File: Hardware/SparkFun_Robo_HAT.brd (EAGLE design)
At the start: 65 x 56.5 mm, 236 parts, among them J11 EXT MTR PWR, J18 ISP, J2 RASPBERRYPI-40-PIN-GPIO_PTH_N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, J20 USB C, J23 CORTEX_JTAG_DEBUG_PTH, J7 EXT SERVO PWR, J8 EXT 5V PWR, Q1 310mA/60V/1.6Ω, Q23 20V/0.2A/8MHz/1.2Ω/1Vth, Q24 20V/0.2A/8MHz/1.2Ω/1Vth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

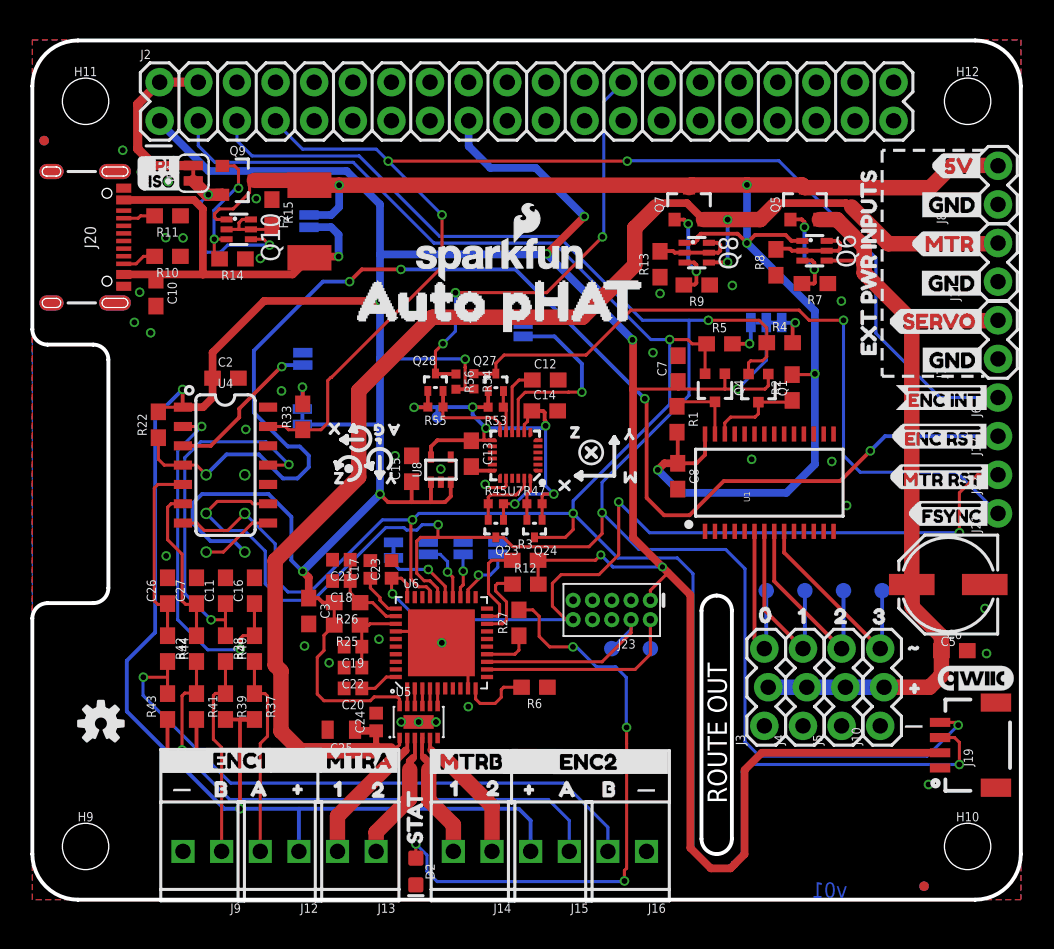
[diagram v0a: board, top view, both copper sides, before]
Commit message: post double-check changes - ready for proto v01
-moved TP6 to SMT pad style and on grid
-updated tran-14386 (ideal diode) to have polarity mark outside package
-nudged vias to avoid silk labels
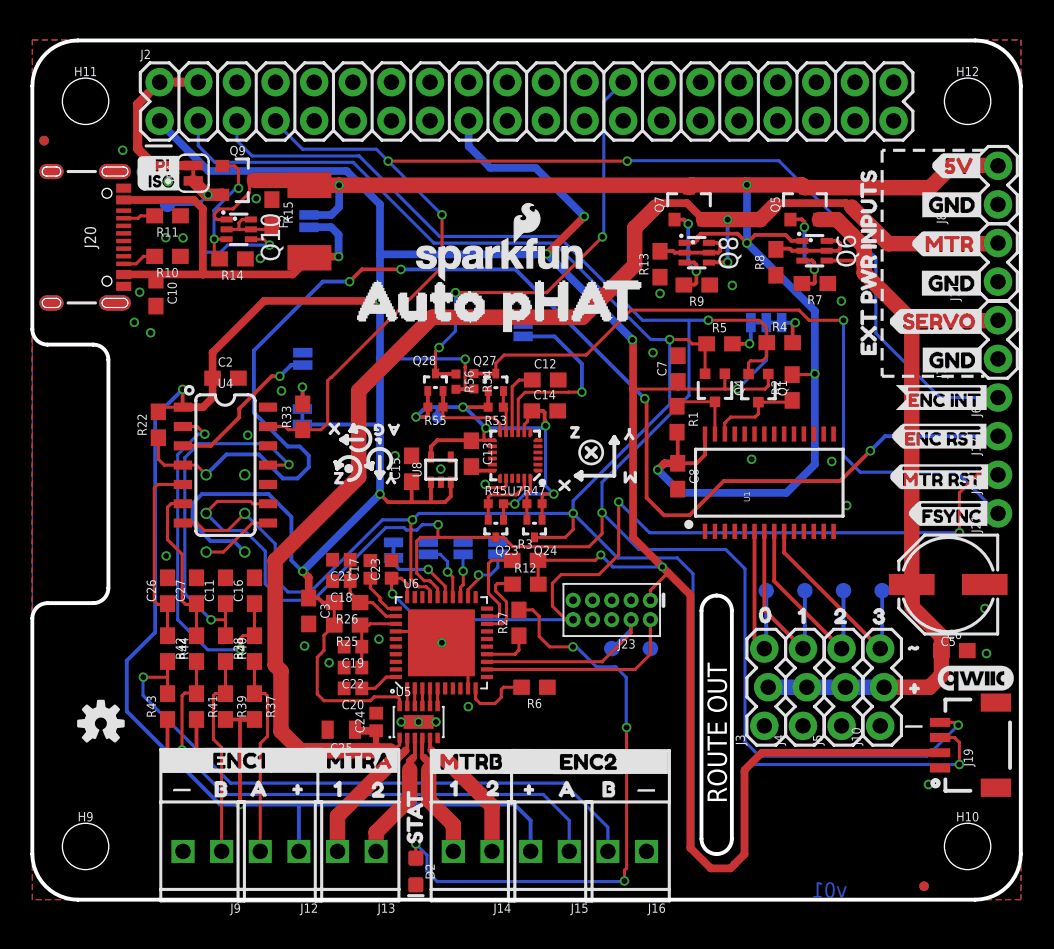
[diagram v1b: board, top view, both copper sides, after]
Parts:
- TP6: value (none) -> TEST-POINT3X4; device SparkFun-Connectors:TP_15TH -> SparkFun-Connectors:PAD.03X.04
- moved TP6 2.76 mm to (8.89, 45.7)
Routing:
- net PI-5V: track 13.1 -> 14.4 mm, vias 1 -> 2
- net 1.8V: track 35.7 -> 36.6 mm

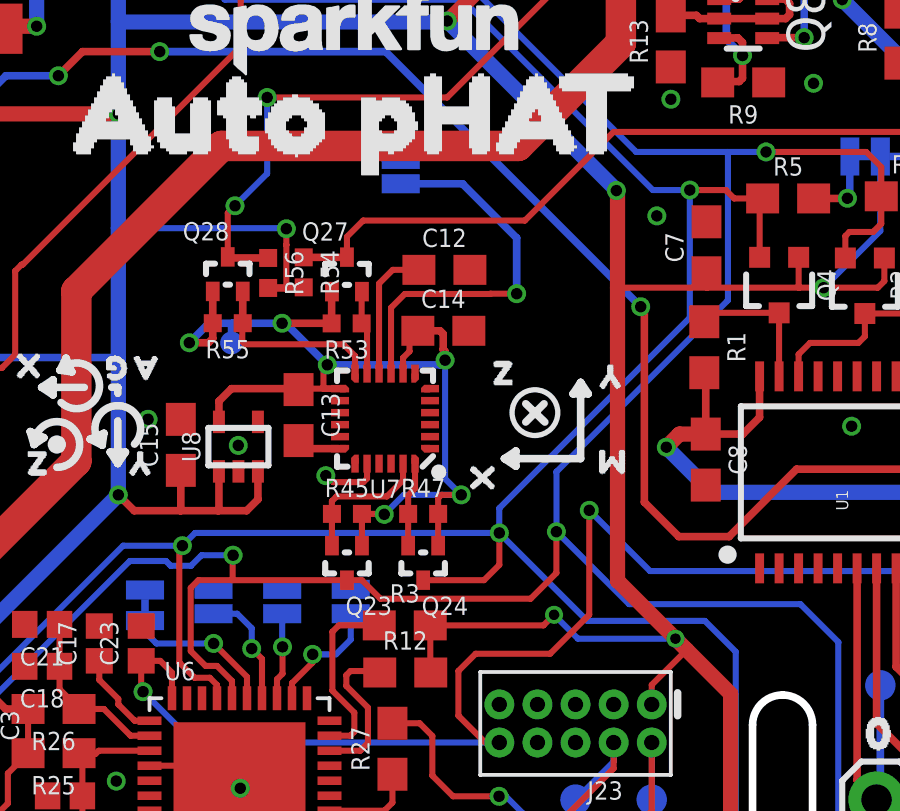
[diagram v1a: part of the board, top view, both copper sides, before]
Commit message: Connected IMU CS pin to 1.8V, Added IMU ADR PU 2.2K resistor
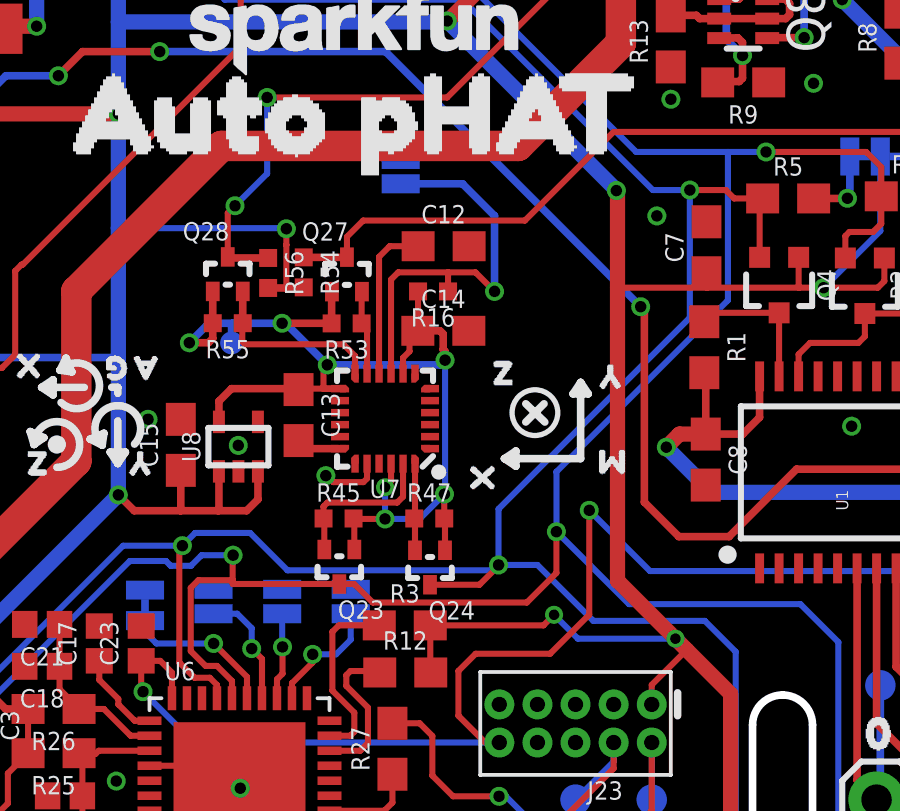
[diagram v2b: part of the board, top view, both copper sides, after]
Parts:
- added R16: 2.2k, SparkFun-Resistors:0402-TIGHT
- moved C12 0.79 mm to (33.7, 35.0)
- moved R45 0.32 mm to (30.2, 25.9)
- moved Q23 0.28 mm to (30.2, 23.7)
- moved Q24 0.27 mm to (33.2, 23.7)
- moved R47 0.25 mm to (33.2, 25.9)
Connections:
- net 1.8V: now also R16.2, U7.22
- net AD0/SDO: now also R16.1
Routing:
- net 1.8V: track 36.6 -> 38.9 mm, vias 6 -> 7
- net N$29: track 4.52 -> 5.34 mm
- net SCL_1.8V: track 4.70 -> 5.33 mm
- net AD0/SDO: track 13.1 -> 13.7 mm

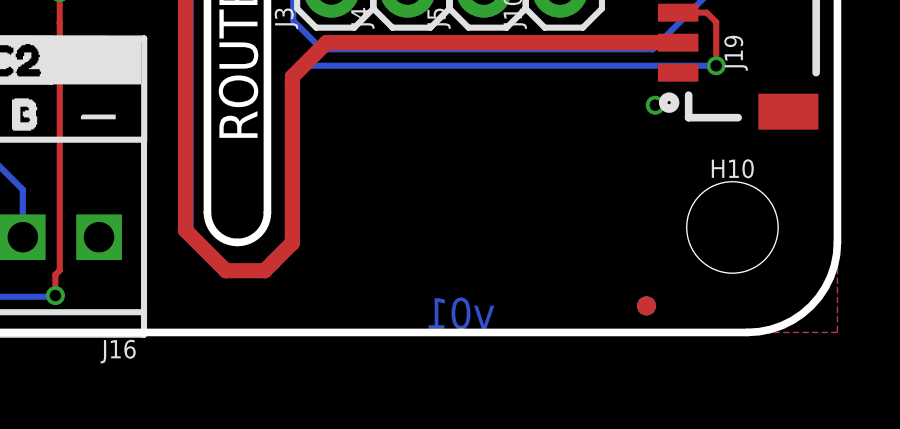
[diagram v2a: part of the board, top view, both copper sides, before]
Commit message: bumped version to v10 in sch and brd
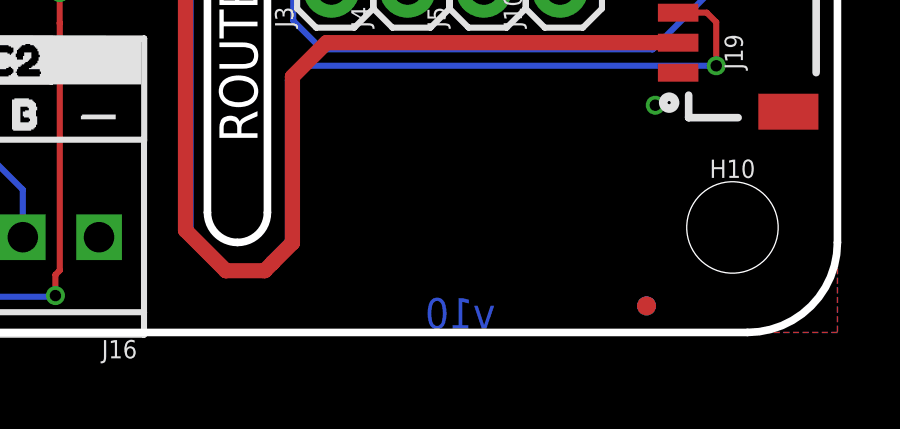
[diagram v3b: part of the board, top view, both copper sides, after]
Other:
- board text added: "v10"
- board text removed: "v01"
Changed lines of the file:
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@@
 <rectangle x1="7.40918125" y1="47.767240625" x2="7.79525625" y2="48.894996875" layer="21"/>
 <rectangle x1="9.21511875" y1="47.75708125" x2="9.65961875" y2="48.91024375" layer="21"/>
-<text x="53.594" y="0.127" size="1.016" layer="16" font="vector" ratio="20" rot="SMR0">v01</text>
+<text x="53.594" y="0.127" size="1.016" layer="16" font="vector" ratio="20" rot="SMR0">v10</text>
 <text x="45.669196875" y="6.33221875" size="1.27" layer="20" font="vector" ratio="12" rot="R90">ROUTE OUT</text>
 <circle x="20.810221875" y="28.348940625" radius="0.3048" width="0" layer="21"/>

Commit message: moving to SMD stackable solution... 99 done
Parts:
- J19: value (none) -> QWIIC_RIGHT_ANGLE; device SparkFun-Connectors:1X04_1MM_RA -> SparkFun-Connectors:JST04_1MM_RA
- J2: value RASPBERRYPI-40-PIN-GPIO_PTH_NO_SHROUD -> RASPBERRYPI-40-PIN-GPIO_SMD_STACKABLE; device SparkFun-Connectors:2X20 -> SparkFun-Connectors:RASPBERRY_PI_HAT_40_PIN_SMD_STACKABLE
- TP0, TP1, TP2, TP3, TP7, TP8: value (none) -> TEST-POINT3X4
- TP4, TP5: value (none) -> TEST-POINTTP_15TH_THRU
- TP9: value (none) -> TEST-POINT3
- moved TP6 1.27 mm to (8.89, 44.5)
- moved U$32 1.20 mm to (6.86, 46.1)
- moved U$35 1.20 mm to (7.32, 47.1)
- moved JP4 1.15 mm to (10.5, 46.6)
- moved R11 0.79 mm to (8.86, 44.2)
- moved Q9 0.69 mm to (13.5, 46.6)
- moved R15 0.27 mm to (15.9, 45.0)
- moved F2 0.23 mm to (18.2, 44.4)
- moved Q10 0.16 mm to (13.6, 43.9)
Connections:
- new net CE0: J2.24, J2.24B
- new net GP12: J2.32, J2.32B
- new net GP13: J2.33, J2.33B
- new net GP16: J2.36, J2.36B
- new net GP17: J2.11, J2.11B
- new net GP18: J2.12, J2.12B
- new net GP19: J2.35, J2.35B
- new net GP20: J2.38, J2.38B
- new net GP21: J2.40, J2.40B
- new net GP22: J2.15, J2.15B
- new net GP23: J2.16, J2.16B
- new net GP24: J2.18, J2.18B
- new net GP25: J2.22, J2.22B
- new net GP26: J2.37, J2.37B
- new net GP27: J2.13, J2.13B
- new net GP5: J2.29, J2.29B
- new net GP6: J2.31, J2.31B
- new net ID_SC: J2.28, J2.28B
- new net ID_SD: J2.27, J2.27B
- new net PI_MISO: J2.21, J2.21B
- new net PI_MOSI: J2.19, J2.19B
- new net PI_RXI: J2.10, J2.10B
- new net PI_TXO: J2.8, J2.8B
- new net SCLK: J2.23, J2.23B
- net !ENC_INT: now also J2.7B
- net 3.3V: now also J2.17B, J2.1B
- net GND: now also J2.14B, J2.20B, J2.25B, J2.30B, J2.34B, J2.39B, J2.6B, J2.9B
- net IMU_INT_3.3V: now also J2.26B
- net N$20: now also J2.2B, J2.4B
- net SCL_3.3V: now also J2.5B
- net SDA_3.3V: now also J2.3B
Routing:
- net 3.3V: track 313.7 -> 322.1 mm, vias 13 -> 15
- net !ENC_INT: track 84.1 -> 92.1 mm, vias 3 -> 4
- net N$20: track 11.6 -> 19.3 mm, vias 0 -> 1
- net PI_MOSI: track 0.00 -> 4.51 mm, vias 0 -> 1
- net GP27: track 0.00 -> 4.51 mm, vias 0 -> 1
- net GP17: track 0.00 -> 4.51 mm, vias 0 -> 1
- net ID_SD: track 0.00 -> 4.51 mm, vias 0 -> 1
- net GP5: track 0.00 -> 4.51 mm, vias 0 -> 1
- net SCLK: track 0.00 -> 4.46 mm, vias 0 -> 1
- net PI_MISO: track 0.00 -> 4.46 mm, vias 0 -> 1
- net GP6: track 0.00 -> 4.46 mm, vias 0 -> 1
- net GP22: track 0.00 -> 4.46 mm, vias 0 -> 1
- net GP26: track 0.00 -> 4.41 mm, vias 0 -> 1
- net GP19: track 0.00 -> 4.41 mm, vias 0 -> 1
- net GP13: track 0.00 -> 4.36 mm, vias 0 -> 1
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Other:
- board size 65 x 56.5 mm -> 65.1 x 57 mm

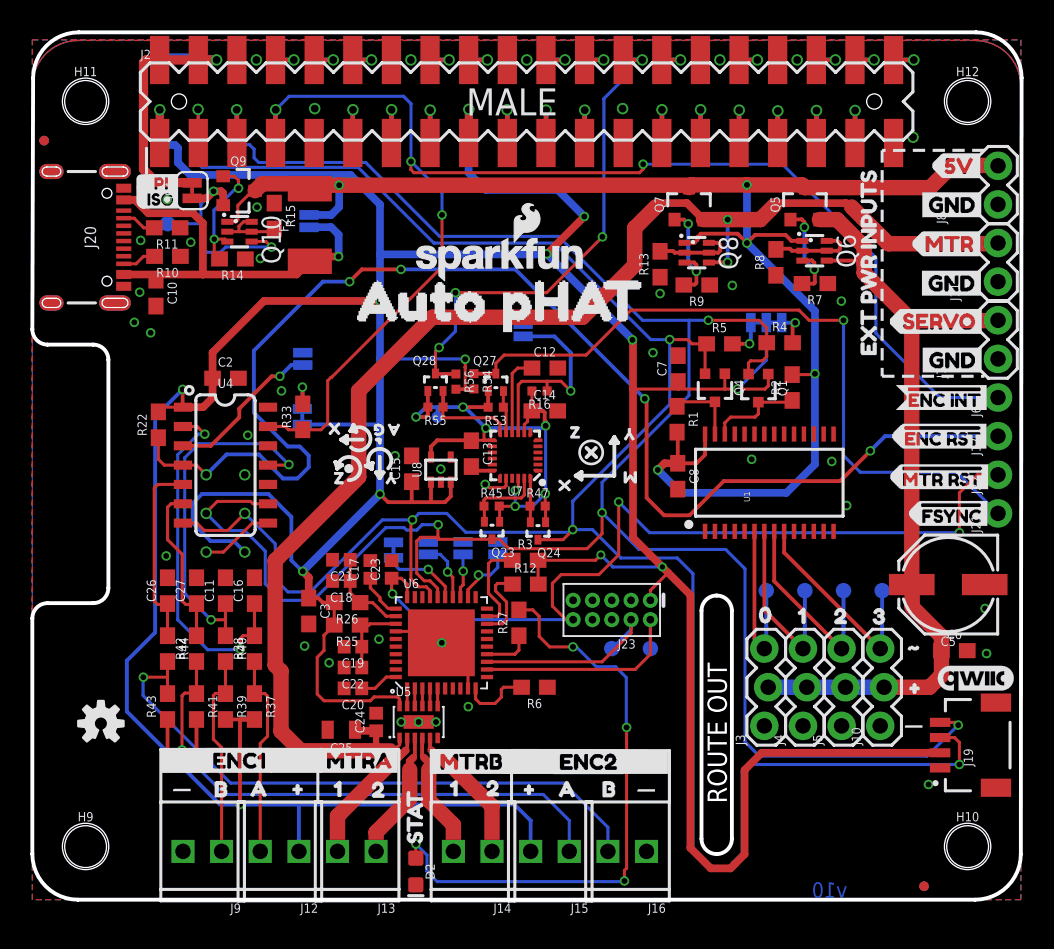
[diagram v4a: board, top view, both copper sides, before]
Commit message: Added LOGO, improved GND pour flowing
-added LOGO to top and bottom silk
-rerouted some traces on right side of board near the EXT headers to allow for better GND flow
-added more gnd vias near SMD pads on stackable header package
-removed pesky test point values in SCH
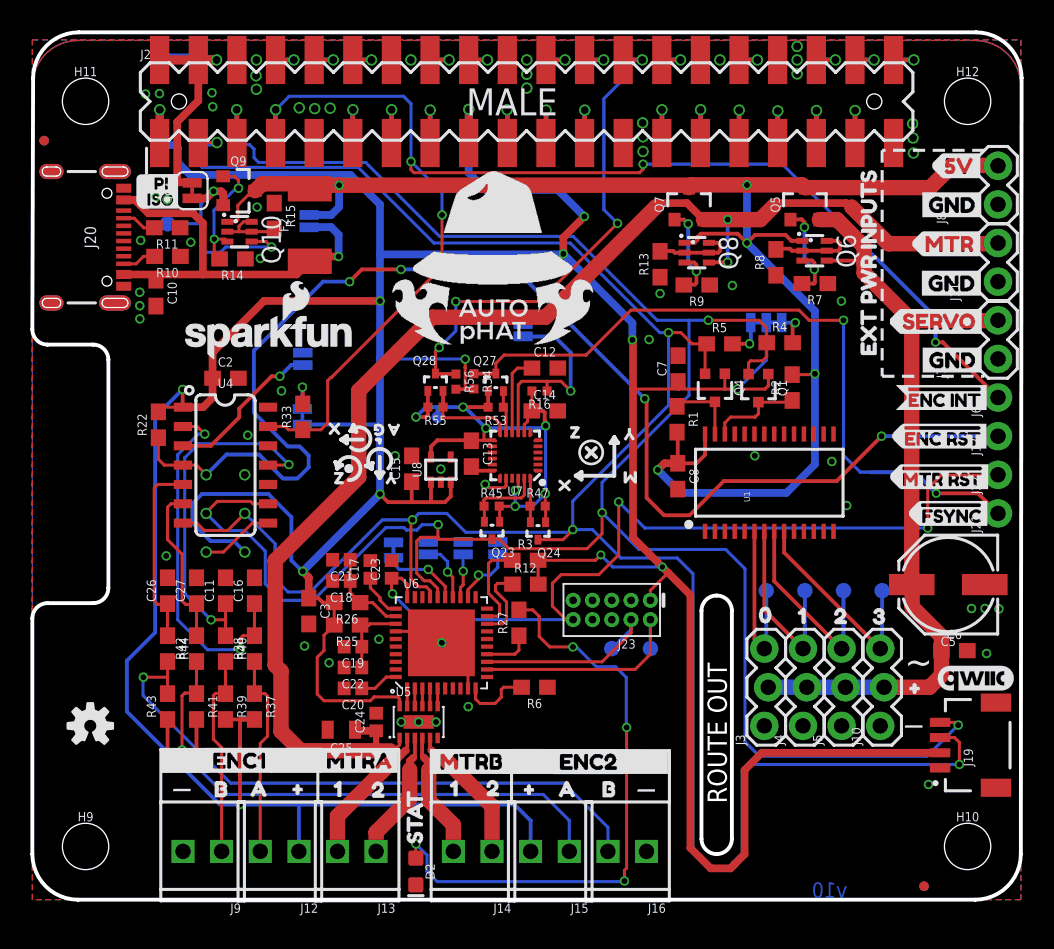
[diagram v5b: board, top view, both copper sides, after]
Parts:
- removed U$42, U$45: (no value), buzzard_labels (5):#4
- removed U$84: (no value), buzzard_labels (9):AUTO_PHAT0
- added U$85: (no value), robohat:AUTOHAT-LOGO
- J19: value QWIIC_RIGHT_ANGLE -> (none)
- J2: value RASPBERRYPI-40-PIN-GPIO_SMD_STACKABLE -> RASPBERRYPI-40-PIN-GPIO_SMD_STACKABLE_NOHOLES; device SparkFun-Connectors:RASPBERRY_PI_HAT_40_PIN_SMD_STACKABLE -> SparkFun-Connectors:RASPBERRY_PI_HAT_40_PIN_SMD_STACKABLE_NOHOLES
- TP0, TP1, TP2, TP3, TP6, TP7, TP8: value TEST-POINT3X4 -> (none)
- TP4, TP5: value TEST-POINTTP_15TH_THRU -> (none)
- TP9: value TEST-POINT3 -> (none)
- U$83: device buzzard_labels (9):AUTO_PHAT0 -> robohat:AUTOHAT-LOGO
- moved U$83 24.6 mm to (42.6, 32.4), flipped to the bottom
- moved LOGO4 16.0 mm to (15.6, 37.0)
- moved LOGO1 2.26 mm to (31.0, 43.8)
- moved LOGO2 0.71 mm to (3.81, 11.4)
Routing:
- net N$20: track 19.3 -> 17.2 mm
- net !ENC_INT: track 92.1 -> 90.1 mm, vias 4 -> 5
- net SDA_3.3V: track 156.3 -> 154.7 mm
- net VIN-MTR: track 91.4 -> 89.9 mm
- net GND: vias 42 -> 60
- net !FSYNC_3.3V: vias 1 -> 2
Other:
- board text added: "~"
